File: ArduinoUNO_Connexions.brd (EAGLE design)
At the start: 167.6 x 130.8 mm, 73 parts

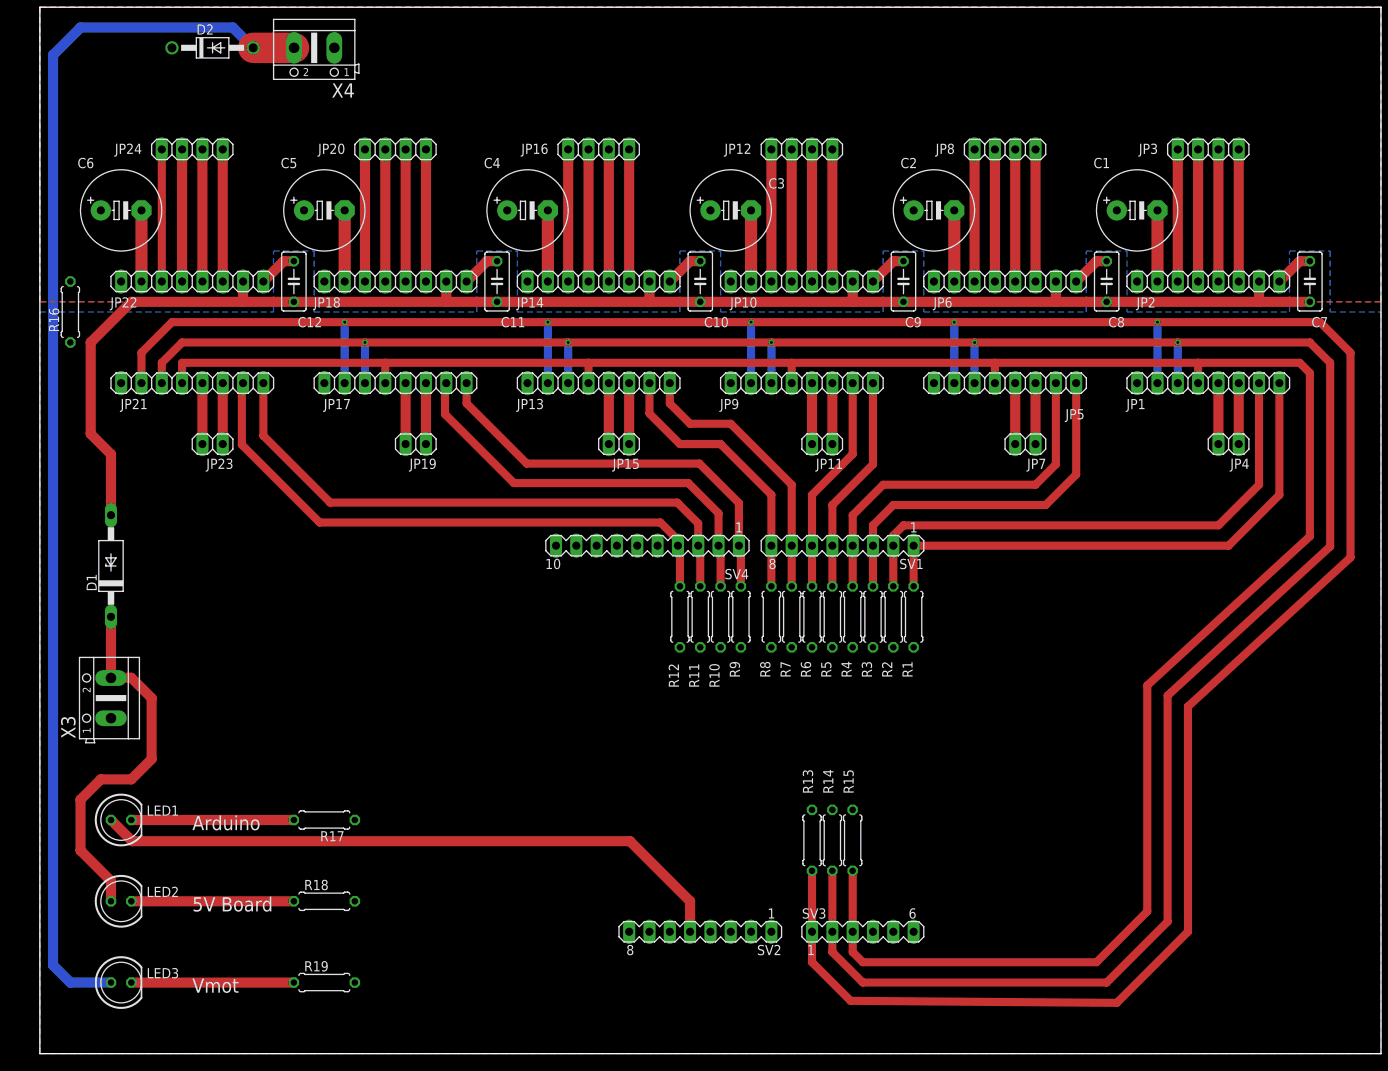
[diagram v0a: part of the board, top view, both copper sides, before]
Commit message: Update board with holee for screws
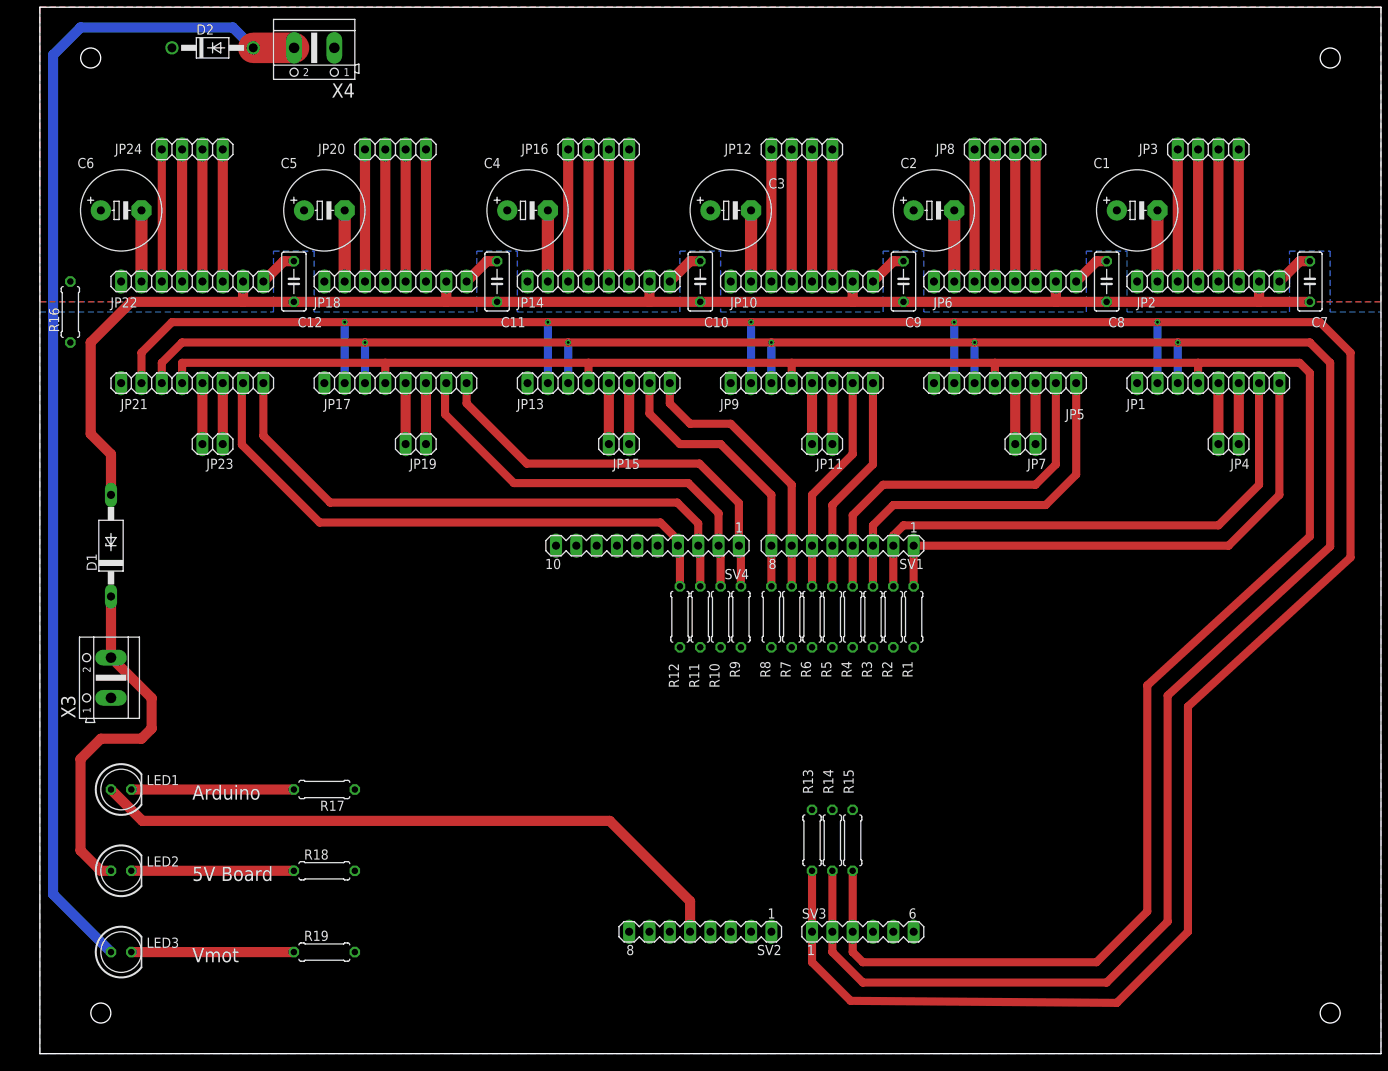
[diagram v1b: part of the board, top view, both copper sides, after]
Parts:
- moved LED1 3.81 mm to (5.08, 26.7)
- moved LED2 3.81 mm to (5.08, 16.5)
- moved R17 3.81 mm to (30.5, 26.7)
- moved R18 3.81 mm to (30.5, 16.5)
- moved LED3 3.81 mm to (5.08, 6.35)
- moved R19 3.81 mm to (30.5, 6.35)
- moved D1 2.54 mm to (3.81, 57.1)
- moved X3 2.54 mm to (3.81, 40.6)
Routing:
- net N$1: track 154.5 -> 147.7 mm
- net VCC: track 192.4 -> 189.8 mm
- net N$3: track 80.4 -> 82.0 mm
- net N$2: track 46.7 -> 45.4 mm

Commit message: update
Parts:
- moved JP11 8.13 mm to (97.8, 76.2)
- moved JP4 8.13 mm to (148.6, 76.2)
- moved JP19 8.13 mm to (47.0, 76.2)
- moved PCB2 8.13 mm to (47.0, -64.8)
- moved R2 8.13 mm to (106.7, 54.6)
- moved D2 8.13 mm to (21.6, 125.7)
- moved JP15 8.13 mm to (72.4, 76.2)
- moved JP23 8.13 mm to (21.6, 76.2)
- moved JP7 8.13 mm to (123.2, 76.2)
- moved X4 8.13 mm to (34.3, 125.7)
- moved C7 8.13 mm to (158.8, 96.5)
- moved JP1 8.13 mm to (146.1, 83.8)
- moved JP2 8.13 mm to (146.1, 96.5)
- moved JP3 8.13 mm to (146.1, 113.0)
- moved JP5 8.13 mm to (120.7, 83.8)
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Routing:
- net DIR$5: track 73.0 -> 77.0 mm
- net VCC: track 189.8 -> 192.5 mm
- net N$3: track 82.0 -> 82.7 mm
- net RESOLUTION$0: track 341.6 -> 341.0 mm
- net RESOLUTION$2: track 283.1 -> 282.6 mm
- net RESOLUTION$1: track 311.7 -> 311.2 mm
- added copper zone on layer 1, net DIR$5
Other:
- board text added: "Pull down resistors"
